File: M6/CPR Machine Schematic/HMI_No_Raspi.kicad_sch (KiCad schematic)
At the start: 12 parts, among them IC1 SPI Tri-State Buffer, SW5 LED Button, SW6 LED Button, SW7 Non-LED Button, U10 Screen Driver 2, U11 Speaker Driver 1, U12 Speaker Driver 2, U9 Screen Driver 1

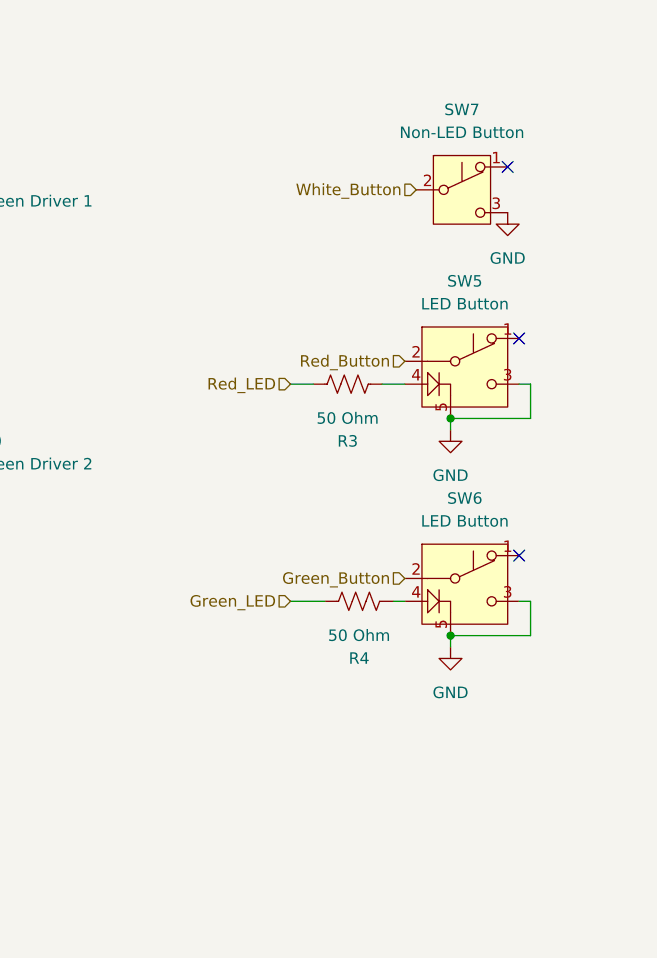
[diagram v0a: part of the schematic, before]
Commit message: force sensor oobs
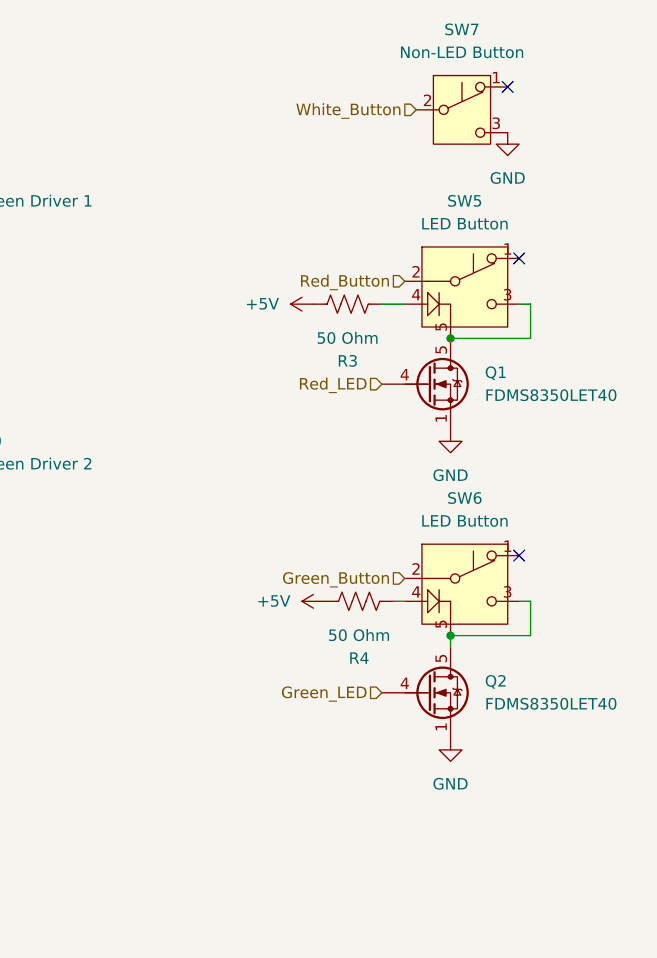
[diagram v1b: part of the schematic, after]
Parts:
- added Q1, Q2: FDMS8350LET40, Package_TO_SOT_SMD:TDSON-8-1, symbol Transistor_FET:FDMS8350LET40
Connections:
- net +5V: now also R3.2, R4.2
- net GND: now also Q1.1 (S), Q1.2 (S), Q1.3 (S), Q2.1 (S), Q2.2 (S), Q2.3 (S); no longer SW5.3 (C), SW5.5 (GND), SW6.3 (C), SW6.5 (GND)
- net Green_LED: now also Q2.4 (G); no longer R4.2
- net Red_LED: now also Q1.4 (G); no longer R3.2
- new net: Q1.5 (D), SW5.3 (C), SW5.5 (GND)
- new net: Q2.5 (D), SW6.3 (C), SW6.5 (GND)
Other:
- moved on the sheet: R3, SW5, SW7

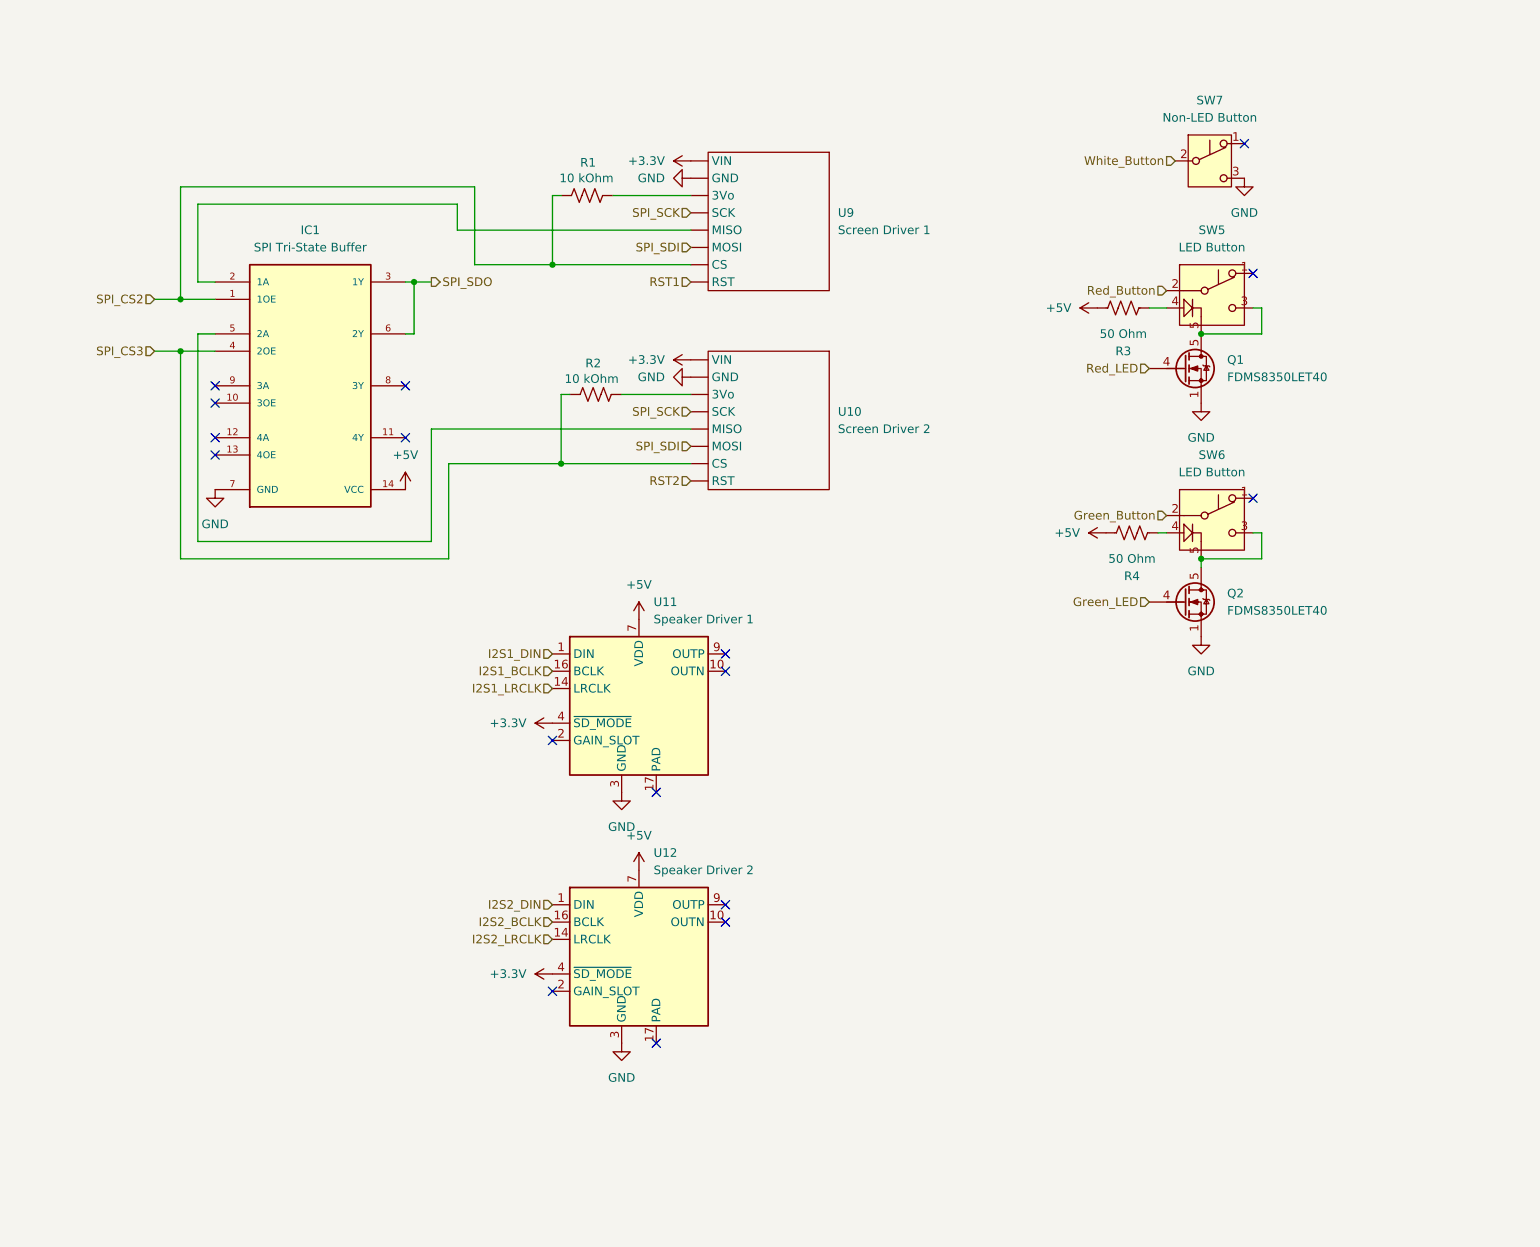
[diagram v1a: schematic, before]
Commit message: I2S Combination and Screen driver fixes
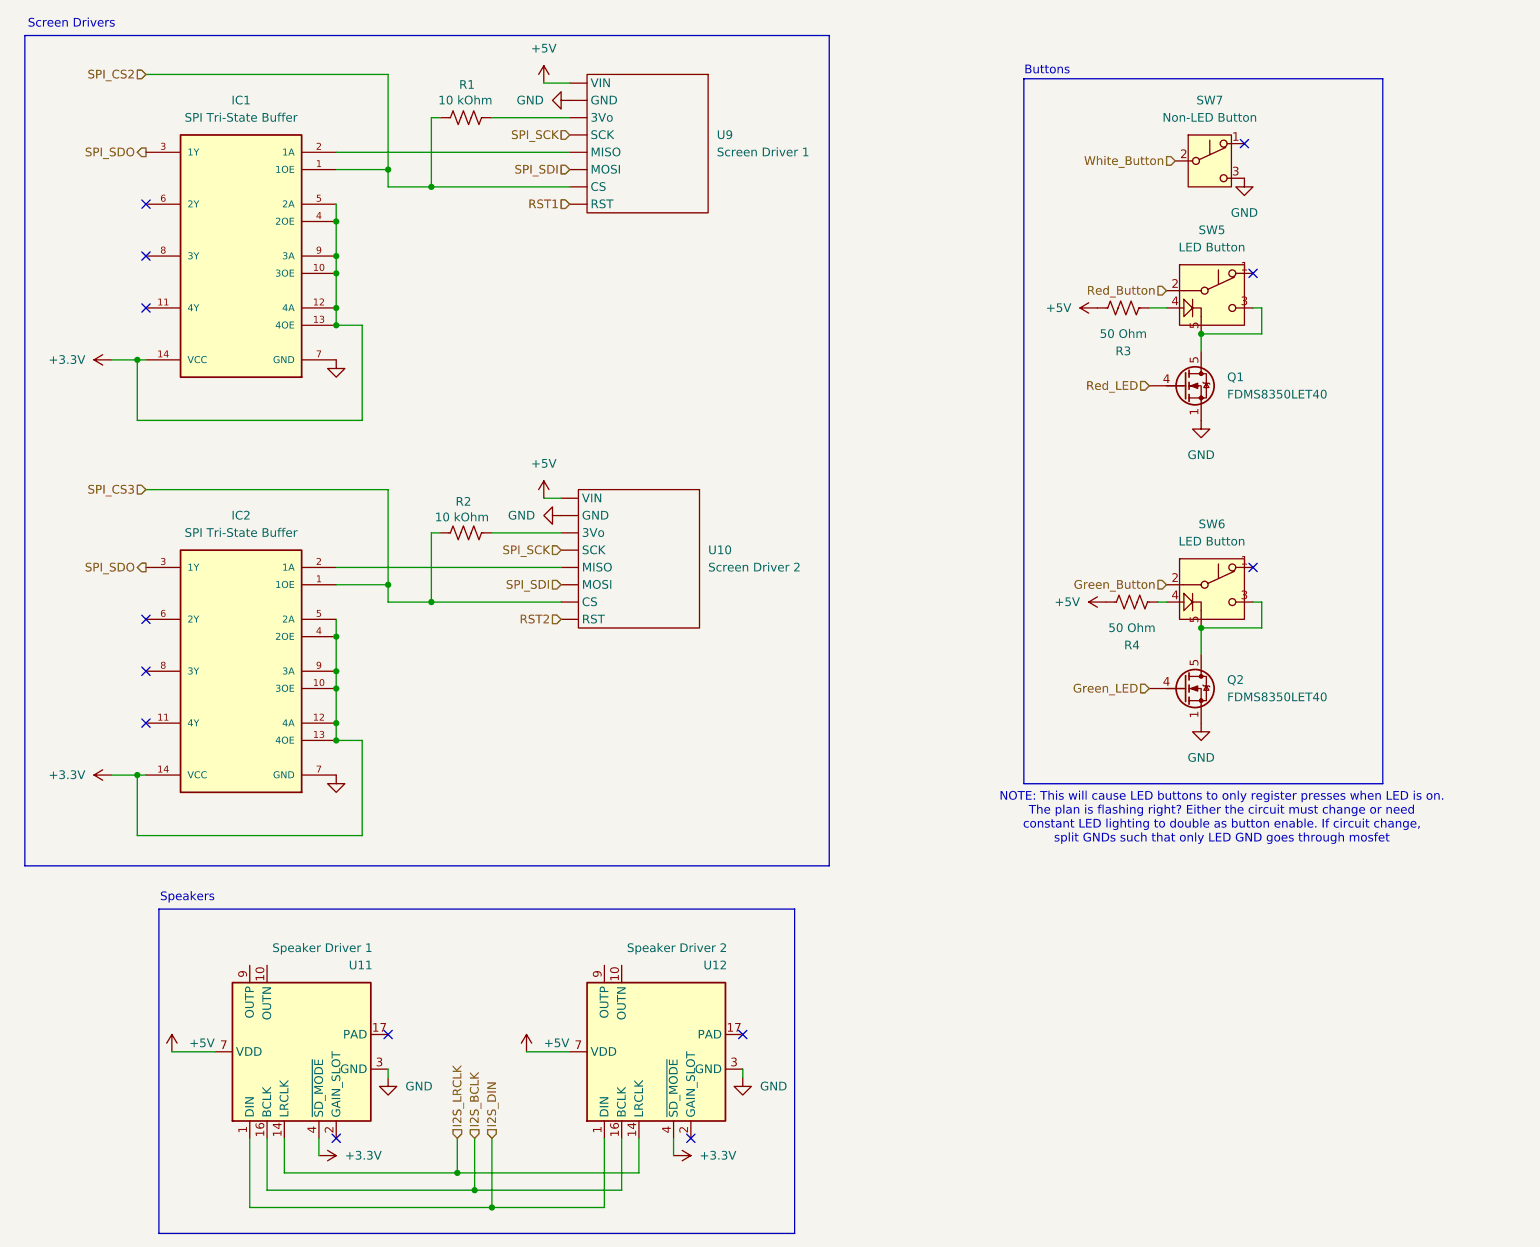
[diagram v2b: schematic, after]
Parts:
- added IC2: SPI Tri-State Buffer, 74HC125:SOIC-14, symbol 74HC125:74HC125
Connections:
- net I2S2_BCLK is gone; now on net I2S_BCLK: U12.16 (BCLK)
- net I2S2_DIN is gone; now on net I2S_DIN: U12.1 (DIN)
- net I2S2_LRCLK is gone; now on net I2S_LRCLK: U12.14 (LRCLK)
- net +3.3V: now also IC1.10 (3OE), IC1.12 (4A), IC1.13 (4OE), IC1.14 (VCC), IC1.4 (2OE), IC1.5 (2A), IC1.9 (3A), IC2.10 (3OE), IC2.12 (4A), IC2.13 (4OE), IC2.14 (VCC), IC2.4 (2OE), IC2.5 (2A), IC2.9 (3A); no longer U10. (RST), U9. (RST)
- net +5V: now also U10. (RST), U9. (RST); no longer IC1.14 (VCC)
- net GND: now also IC2.7 (GND)
- net SPI_CS3: now also IC2.1 (1OE); no longer IC1.4 (2OE)
- net SPI_SDO: now also IC2.3 (1Y); no longer IC1.6 (2Y)
- net I2S1_BCLK renamed I2S_BCLK
- net I2S1_DIN renamed I2S_DIN
- net I2S1_LRCLK renamed I2S_LRCLK
- new net: IC2.2 (1A), U10. (RST)
- no-connect marks 17 -> 13
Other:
- note added: "Buttons"
- note added: "NOTE: This will cause LED buttons to only register presses when LED is on. The plan is flashing right? Either the circuit must change or need constant LED lighting to double as button enable. If circuit change, split GNDs such that only LED GND goes through mosfet"
- note added: "Screen Drivers"
- note added: "Speakers"
- moved on the sheet: IC1, Q1, Q2, R1, R2, R4, SW6, U10, U11, U9

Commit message: more kicad
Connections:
- net RST2 is gone; now on net SPI_SDI: U10. (RST)
- net RST1: now also U10. (RST)
- net SPI_CS2: now also IC2.1 (1OE), R2.1, U10. (RST)
- removed net SPI_CS3: IC2.1 (1OE), R2.1, U10. (RST)
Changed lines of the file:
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@@
+		)
+	)
+	(hierarchical_label "SPI_CS2"
+		(shape input)
+		(at 36.83 87.63 180)
+		(effects
+			(font
+				(size 1.27 1.27)
+			)
+			(justify right)
 		)
 	)
@@
 		)
 	)
-	(hierarchical_label "SPI_CS3"
+	(hierarchical_label "SPI_CS2"
 		(shape input)
-		(at 36.83 87.63 180)
+		(at 36.83 26.67 180)
 		(effects
 			(font
@@
 		)
 	)
-	(hierarchical_label "SPI_CS2"
+	(hierarchical_label "RST1"
 		(shape input)
-		(at 36.83 26.67 180)
+		(at 97.79 106.68 180)
 		(effects
 			(font
@@
 		)
 	)
-	(hierarchical_label "RST2"
-		(shape input)
-		(at 97.79 106.68 180)
-		(effects
-			(font
-				(size 1.27 1.27)
-			)
-			(justify right)
-		)
-	)
